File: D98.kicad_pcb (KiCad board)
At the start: 2 copper layers, 40 x 60 mm, 12 parts, among them J1 Conn_01x02, J2 Conn_01x04, J3 Conn_01x08, J4 Conn_01x06, J5 Conn_01x06, J6 Conn_01x06, J7 Conn_01x05, U2 YAAJ_BluePill_SWD_Breakout, U3 Poka Yoke

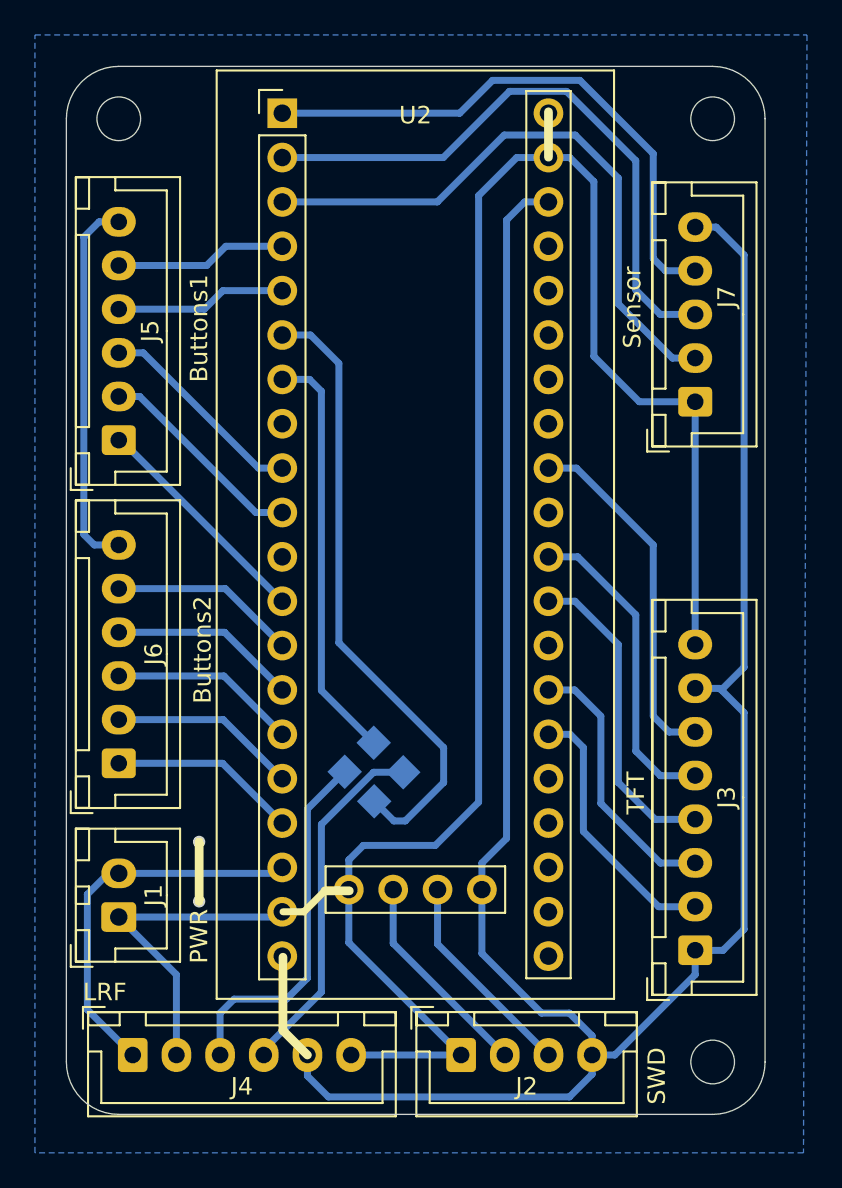
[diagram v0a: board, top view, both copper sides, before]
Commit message: feat: 	changed position of MountingHoles             Small modefication and Rounding Tracks.
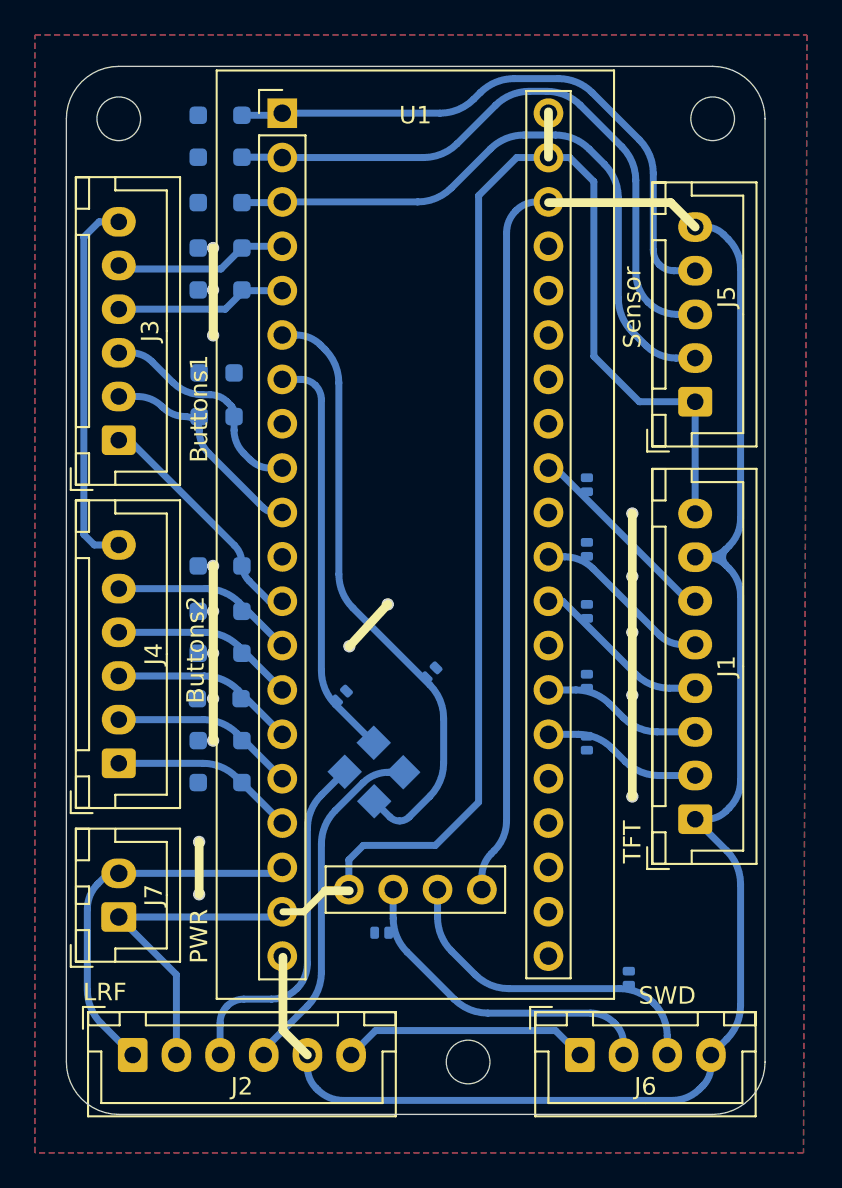
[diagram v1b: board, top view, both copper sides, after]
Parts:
- added D1: LESD8D3.3N3T5G, Diode_SMD:D_SOD-882D, B.Cu at (89.6, 43.8)
- added D10: CESD5V0D3, Diode_SMD:D_SOD-323_HandSoldering, B.Cu at (68.6, 22.6)
- added D11: CESD5V0D3, Diode_SMD:D_SOD-323_HandSoldering, B.Cu at (68.6, 25.0)
- added D12: CESD5V0D3, Diode_SMD:D_SOD-323_HandSoldering, B.Cu at (68.6, 27.6)
- added D13: CESD5V0D3, Diode_SMD:D_SOD-323_HandSoldering, B.Cu at (68.6, 30.2)
- added D14: CESD5V0D3, Diode_SMD:D_SOD-323_HandSoldering, B.Cu at (68.6, 32.6)
- added D15: CESD5V0D3, Diode_SMD:D_SOD-323_HandSoldering, B.Cu at (69.4, 38.6)
- added D16: CESD5V0D3, Diode_SMD:D_SOD-323_HandSoldering, B.Cu at (67.4, 38.6)
- added D17: CESD5V0D3, Diode_SMD:D_SOD-323_HandSoldering, B.Cu at (68.6, 48.4)
- added D18: CESD5V0D3, Diode_SMD:D_SOD-323_HandSoldering, B.Cu at (68.6, 51.0)
- added D19: CESD5V0D3, Diode_SMD:D_SOD-323_HandSoldering, B.Cu at (68.6, 53.4)
- added D2: LESD8D3.3N3T5G, Diode_SMD:D_SOD-882D, B.Cu at (89.6, 47.5)
- added D20: CESD5V0D3, Diode_SMD:D_SOD-323_HandSoldering, B.Cu at (68.5, 56.0)
- added D21: CESD5V0D3, Diode_SMD:D_SOD-323_HandSoldering, B.Cu at (68.6, 58.4)
- added D22: CESD5V0D3, Diode_SMD:D_SOD-323_HandSoldering, B.Cu at (68.6, 60.8)
- added D3: LESD8D3.3N3T5G, Diode_SMD:D_SOD-882D, B.Cu at (89.6, 51.0)
- added D4: LESD8D3.3N3T5G, Diode_SMD:D_SOD-882D, B.Cu at (89.6, 55.0)
- added D5: LESD8D3.3N3T5G, Diode_SMD:D_SOD-882D, B.Cu at (89.6, 58.5)
- added D6: LESD8D3.3N3T5G, Diode_SMD:D_SOD-882D, B.Cu at (92.0, 72.0)
- added D7: LESD8D3.3N3T5G, Diode_SMD:D_SOD-882D, B.Cu at (77.8, 69.4)
- added D8: LESD8D3.3N3T5G, Diode_SMD:D_SOD-882D, B.Cu at (80.7, 54.5)
- added D9: LESD8D3.3N3T5G, Diode_SMD:D_SOD-882D, B.Cu at (75.6, 55.8)
- moved H3 14.0 mm to (82.8, 76.8)
- moved J1 7.50 mm to (95.8, 62.9)
- moved J6 6.80 mm to (89.2, 76.4)
- renumbered J3 to J1, J4 to J2, J5 to J3, J6 to J4, J7 to J5, J2 to J6, J1 to J7, U2 to U1, U3 to U2
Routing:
- net GND: track 153.5 -> 138.1 mm, vias 2 -> 17
- net MOSI-A7: track 20.4 -> 11.5 mm
- net CLK-A5: track 18.2 -> 10.3 mm
- net CS-A4: track 18.2 -> 10.3 mm
- net SWDIO: track 12.1 -> 19.4 mm
- net SWDCLK: track 12.1 -> 19.1 mm
- net RES-A2: track 15.4 -> 9.13 mm
- net DC-A1: track 15.3 -> 9.12 mm
- net MISO-B14: track 34.6 -> 36.7 mm
- net CS-B12: track 32.4 -> 34.3 mm
- net CLK-B13: track 34.8 -> 36.4 mm
- net En-3.3v: track 137.8 -> 138.9 mm
- net BTN-A12: track 12.1 -> 12.8 mm
- net Tx-A9: track 35.8 -> 35.1 mm
- net BTN-B4: track 13.2 -> 13.7 mm
- added copper zone on F.Cu, net GND

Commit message: Fix:  -SWD pins wasn't installed correctlly now the connection is correct. 		-adding some pin assignment in the back side.
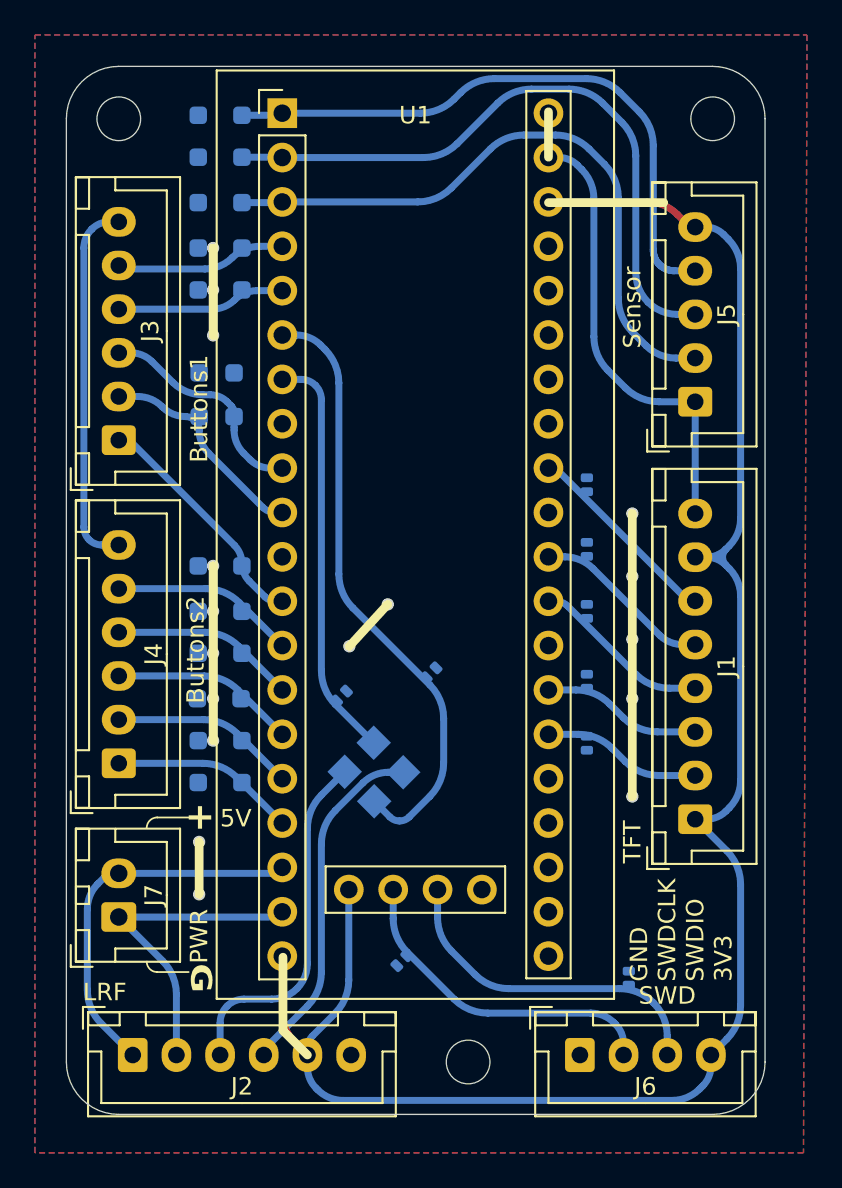
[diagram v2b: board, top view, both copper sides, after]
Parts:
- moved D7 1.97 mm to (79.0, 71.0), turned to -135 degrees
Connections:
- U1 pad 41: En-3.3v -> GND
- U1 pad 44: GND -> En-3.3v
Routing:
- net GND: track 138.1 -> 68.5 mm
- net En-3.3v: track 138.9 -> 107.2 mm
- net CS-B12: track 34.3 -> 35.2 mm
- net CLK-B13: track 36.4 -> 37.3 mm
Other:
- board text added: "+"
- board text added: "3V3"
- board text added: "3v3"
- board text added: "5V"
- board text added: "A12"
- board text added: "A15"
- board text added: "A8"
- board text added: "B15"
- board text added: "B4"
- board text added: "B5"
- board text added: "B6"
- board text added: "B7"
- board text added: "B8"
- board text added: "B9"
- board text added: "BTN-A12"
- board text added: "BTN-A15"
- board text added: "BTN-A8"
- board text added: "BTN-B15"
- board text added: "BTN-B4"
- board text added: "BTN-B5"
- board text added: "BTN-B6"
- board text added: "BTN-B7"
- board text added: "BTN-B8"
- board text added: "BTN-B9"
- board text added: "CLK"
- board text added: "CLK-A5"
- board text added: "CLK-B13"
- board text added: "CS"
- board text added: "CS-A4"
- board text added: "CS-B12"
- board text added: "DC"
- board text added: "DC-A1"
- board text added: "G"
- board text added: "GND"
- board text added: "GND SWDCLK SWDIO 3V3"
- board text added: "MISO"
- board text added: "MISO-B14"
- board text added: "MOSI"
- board text added: "MOSI-A7"
- board text added: "RES"
- board text added: "RES-A2"
- board text added: "Rx"
- board text added: "Rx-Tx"
- board text added: "SWDIO"
- board text added: "Tx"
- board text added: "Tx-Rx"
- board text added: "VIN"

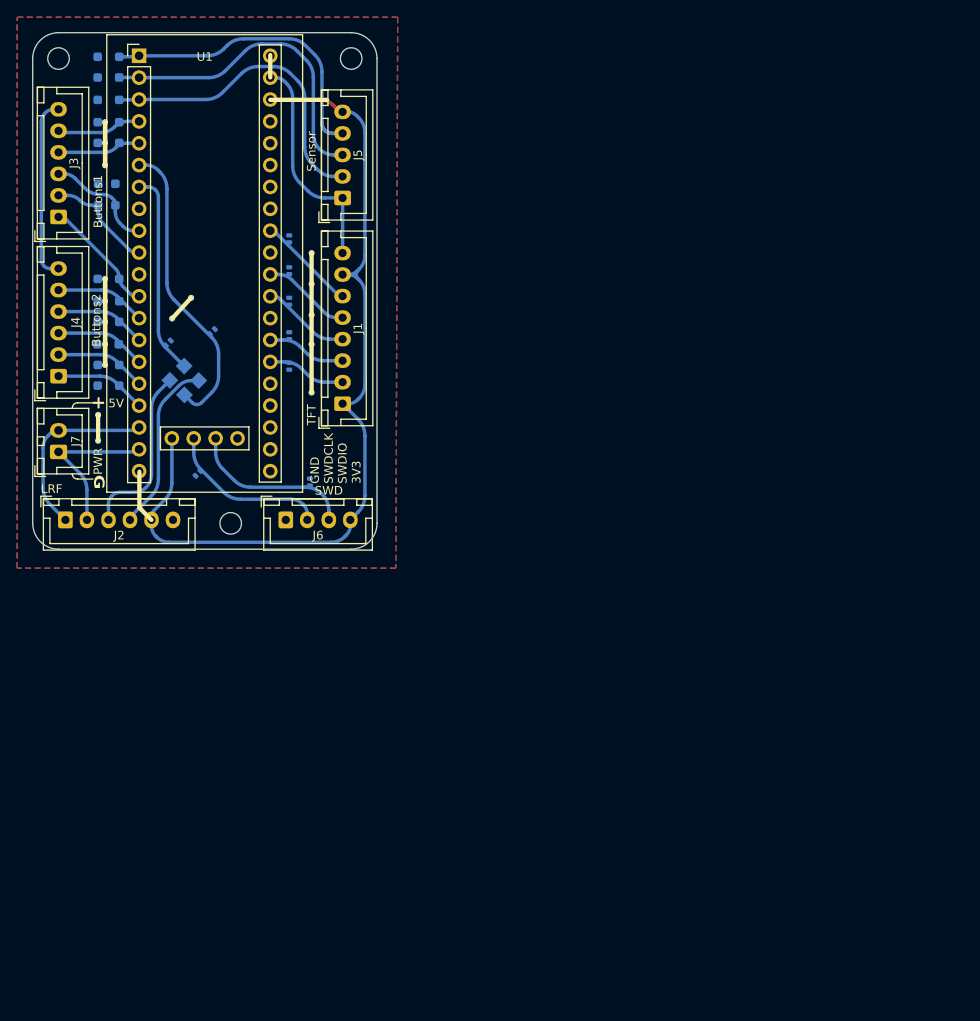
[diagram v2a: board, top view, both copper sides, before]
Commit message: Feat & Edit: changer the position of the TVSes & adding Connector.
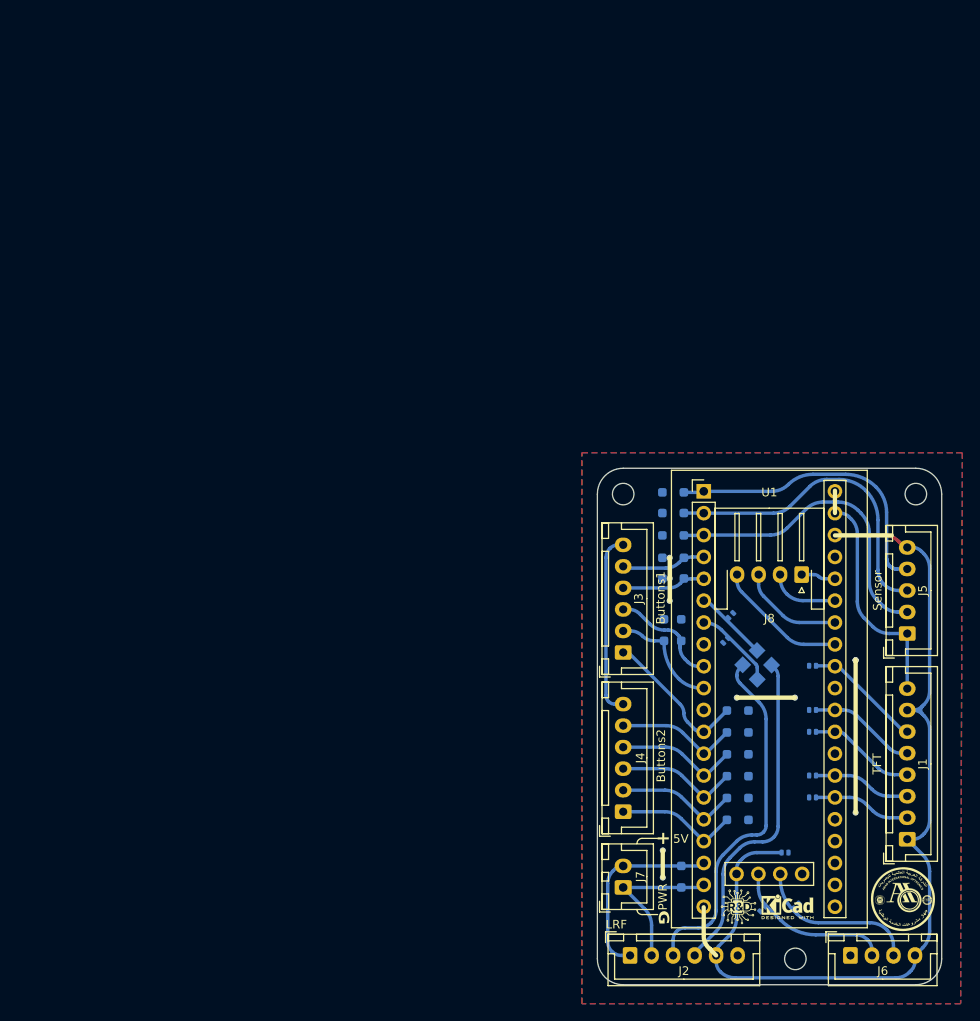
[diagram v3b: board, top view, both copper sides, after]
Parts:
- added D23: CESD5V0D3, Diode_SMD:D_SOD-323_HandSoldering, B.Cu at (135.2, 117.8)
- added D24: LESD8D3.3N3T5G, Diode_SMD:D_SOD-882D, B.Cu at (147.2, 115.0)
- added G***: LOGO, LOGO, F.Cu at (141.8, 121.6)
- added G***: LOGO, LOGO, F.Cu at (160.9, 120.5)
- added G***: LOGO, LOGO, B.Cu at (146.8, 75.5)
- added J8: Conn_01x04, Connector_JST:JST_XH_S4B-XH-A-1_1x04_P2.50mm_Horizontal, F.Cu at (149.1, 82.8)
- added REF**: KiCad-Logo2_5mm_SilkScreen, Symbol:KiCad-Logo2_5mm_SilkScreen, F.Cu at (147.5, 121.3)
- added REF**: KiCad-Logo2_5mm_SilkScreen, Symbol:KiCad-Logo2_5mm_SilkScreen, B.Cu at (134.4, 106.5)
- added REF**: WEEE-Logo_4.2x6mm_SilkScreen, Symbol:WEEE-Logo_4.2x6mm_SilkScreen, B.Cu at (157.6, 74.3)
- added REF**: ESD-Logo_6.6x6mm_SilkScreen, Symbol:ESD-Logo_6.6x6mm_SilkScreen, B.Cu at (158.5, 117.8)
- moved D22 88.8 mm to (141.7, 111.2), turned to 0 degrees
- moved D21 88.7 mm to (141.7, 108.7), turned to 0 degrees
- moved D20 88.7 mm to (141.7, 106.2), turned to 0 degrees
- moved D19 88.7 mm to (141.7, 103.6), turned to 0 degrees
- moved D17 88.6 mm to (141.7, 98.5), turned to 0 degrees
- moved D18 88.6 mm to (141.7, 101.1), turned to 0 degrees
- moved D15 83.0 mm to (135.1, 89.2)
- moved D16 83.0 mm to (133.1, 89.2)
- moved H1 82.8 mm to (128.4, 73.4)
- moved H2 82.8 mm to (162.4, 73.4)
- moved H3 82.8 mm to (148.4, 127.4)
- moved J1 82.8 mm to (161.4, 113.5)
- moved D10 82.8 mm to (134.2, 73.2)
- moved D11 82.8 mm to (134.2, 75.6)
- moved D12 82.8 mm to (134.2, 78.2)
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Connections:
- U1 pad 33: unconnected-(U1-PB0-Pad33) -> SW-B0
- U1 pad 34: unconnected-(U1-PB1-Pad34) -> SW-B1
- U1 pad 35: unconnected-(U1-PB10-Pad35) -> SW-B10
- U1 pad 36: unconnected-(U1-PB11-Pad36) -> SW-B11
- U2 pad 1: Tx-A9 -> Rx-A10
- U2 pad 2: Rx-A10 -> Tx-A9
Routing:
- net Tx-A9: track 35.1 -> 8.58 mm
- net Net-(J2-Pin_3): track 20.5 -> 42.0 mm
- net Net-(J2-Pin_4): track 20.1 -> 39.0 mm
- net SW-B0: track 0.00 -> 15.4 mm
- net Rx-A10: track 23.6 -> 9.72 mm
- net SW-B1: track 0.00 -> 12.1 mm
- net SW-B10: track 0.00 -> 8.24 mm
- net GND: track 68.5 -> 75.3 mm, vias 17 -> 10
- net En-3.3v: track 107.2 -> 113.9 mm
- net SW-B11: track 0.00 -> 3.99 mm
- net BTN-B8: track 10.6 -> 14.3 mm
- net BTN-B7: track 10.6 -> 14.3 mm
- net BTN-B5: track 10.6 -> 14.3 mm
- net BTN-B9: track 10.6 -> 14.4 mm
- net BTN-B6: track 10.6 -> 14.3 mm
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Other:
- board text added: "B0"
- board text added: "B1"
- board text added: "B10"
- board text added: "B11"
- board text added: "Brightness"
- board text added: "Buttons1"
- board text added: "Buttons2"
- board text added: "LRF"
- board text added: "POWER"
- board text added: "SWD"
- board text added: "Sensor"
- board text added: "TFT"
- board text removed: "GND SWDCLK SWDIO 3V3"
